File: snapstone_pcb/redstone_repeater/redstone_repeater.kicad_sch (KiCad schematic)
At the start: 0 parts

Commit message: Actual stuff is in the repeater file now
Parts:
- added C1, C2: 100 µF, symbol Device:C
- added C3: 150 µF, symbol Device:C
- added C4: 200 µF, symbol Device:C
- added R1: 500 ohms, symbol Device:R_US
- added R2, R3, R4: 1000 ohms, symbol Device:R_US
- added SW1, SW2, SW3, SW4: SW_Push, symbol Switch:SW_Push
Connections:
- new net: R2.1, SW2.2
- new net: C2.1, R2.2
- new net: R3.1, SW3.2
- new net: C3.1, R3.2
- new net: R1.1, SW1.2
- new net: C1.1, R1.2
- new net: SW1.1, SW2.1, SW3.1, SW4.1
- new net: C4.1, R4.2
- new net: R4.1, SW4.2
- new net GND: C1.2, C2.2, C3.2, C4.2

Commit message: Worked abit on the resistor
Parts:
- added C5: ~, symbol snapstone:3_Pin_Block_Connector
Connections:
- net GND: now also C5.2 (GND)
- net DAT: now reaches C2.1, R2.2
- net DAT: now also C1.1, C3.1, C4.1, R1.2, R3.2, R4.2
- net at SW1.1, SW2.1, SW3.1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: now also C5.3 (DAT)
- new net VCC: C5.1 (VCC)

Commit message: oops!
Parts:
- added C6, C7: ~, symbol snapstone:3_Pin_Block_Connector
- added R5: 150 ohms, symbol Device:R_US
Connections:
- net DAT: now also C6.3 (DAT)
- net GND: now also C6.2 (GND), C7.2 (GND)
- net VCC: now also C7.1 (VCC)
- new net: C7.3 (DAT), R5.1
- new net: C6.1 (VCC), R5.2

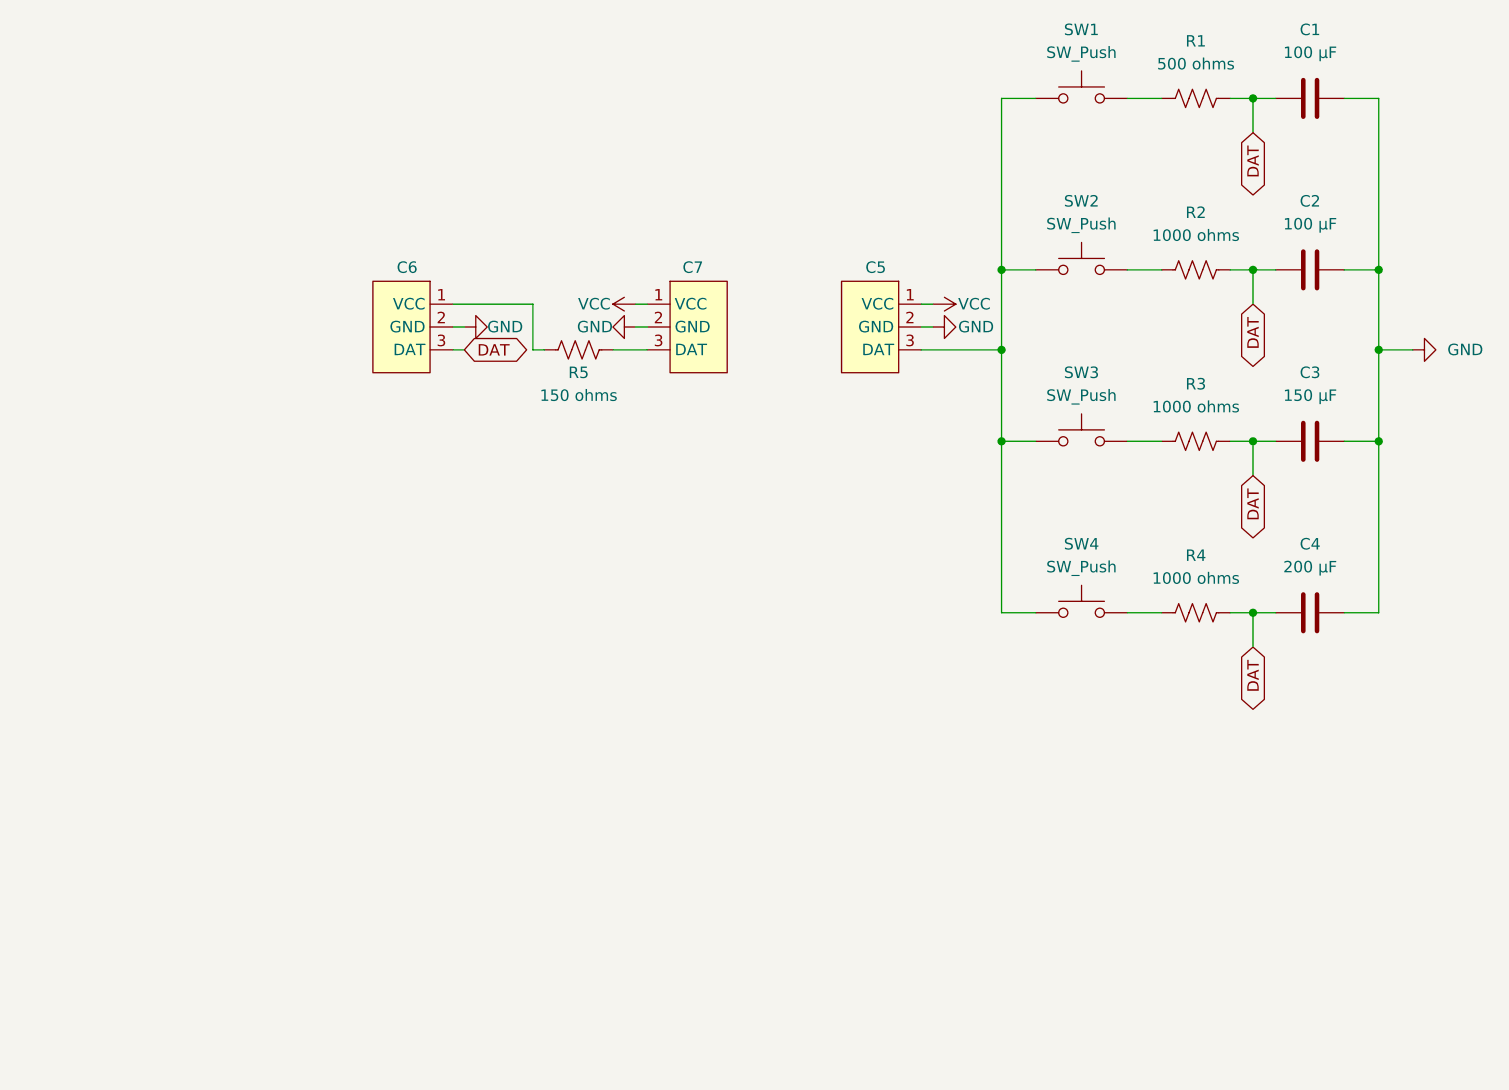
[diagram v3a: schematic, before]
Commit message: Worked on Comparator, gave it DigiPot, gave Repeater schematic a note
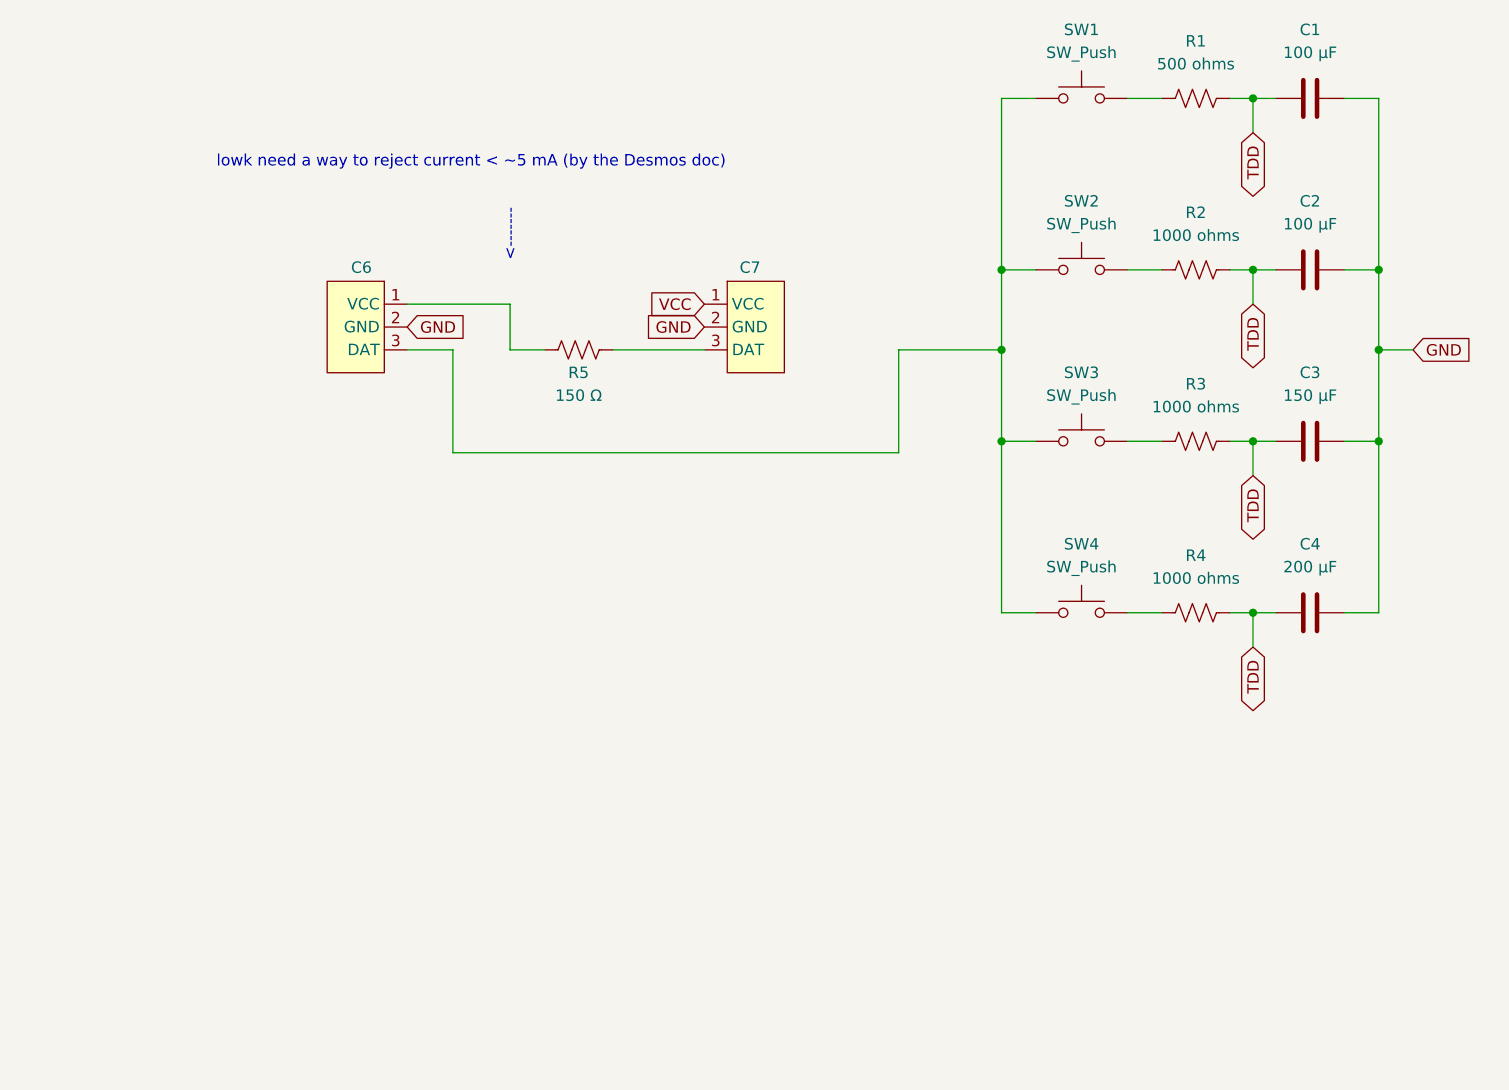
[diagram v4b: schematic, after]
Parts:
- removed C5: ~, symbol snapstone:3_Pin_Block_Connector
- R5: value 150 ohms -> 150 Ω
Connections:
- net at SW1.1, SW2.1, SW3.1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: now also C6.3 (DAT)
- net DAT renamed TDD
- net TDD: no longer C6.3 (DAT)
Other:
- note added: "<-------"
- note added: "lowk need a way to reject current < ~5 mA (by the Desmos doc)"
- moved on the sheet: C6, C7

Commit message: Polished up and maybe done repeater schematic????
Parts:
- added J1: ACS712 Current Sensor, symbol Connector:Conn_01x03_Socket
- added U1: MOUDLE-SEEEDUINO-XIAO, symbol XIAO_RP2040:MOUDLE-SEEEDUINO-XIAO
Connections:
- net GND: now also J1.3 (Pin_3), U1.13 (GND)
- net TDD: now also U1.2 (PA4_A1_D1)
- net VCC: now also C6.1 (VCC), R5.2, J1.1 (Pin_1), U1.12 (3V3)
- net DAT: now reaches C6.3 (DAT), SW1.1, SW2.1, SW3.1, SW4.1
- new net AOUT: J1.2 (Pin_2), U1.1 (PA02_A0_D0)
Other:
- note added: "CURRENT RESET"
- note added: "CURRENT SENSOR"
- note added: "DELAY SWITCH THING"
- note removed: "<-------"
- note removed: "lowk need a way to reject current < ~5 mA (by the Desmos doc)"
- moved on the sheet: C1, C2, C3, C4, C6, C7, R1, R2, R3, R4, R5, SW1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

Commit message: fixed DRC
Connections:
- no-connect marks 0 -> 10
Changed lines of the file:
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@@
+	)
+	(junction
+		(at 140.97 110.49)
+		(diameter 0)
+		(color 0 0 0 0)
 	)
 	(junction
@@
 	)
 	(junction
+		(at 140.97 113.03)
+		(diameter 0)
+		(color 0 0 0 0)
+	)
+	(junction
 		(at 171.45 93.98)
 		(diameter 0)
@@
 		(color 0 0 0 0)
 	)
+	(no_connect
+		(at 138.43 118.11)
+	)
+	(no_connect
+		(at 138.43 107.95)
+	)
+	(no_connect
+		(at 138.43 120.65)
+	)
+	(no_connect
+		(at 138.43 115.57)
+	)
+	(no_connect
+		(at 97.79 118.11)
+	)
+	(no_connect
+		(at 97.79 113.03)
+	)
+	(no_connect
+		(at 138.43 123.19)
+	)
+	(no_connect
+		(at 97.79 120.65)
+	)
+	(no_connect
+		(at 97.79 123.19)
+	)
+	(no_connect
+		(at 97.79 115.57)
+	)
 	(wire
 		(pts
@@
 	(wire
 		(pts
+			(xy 140.97 113.03) (xy 138.43 113.03)
+		)
+		(stroke
+			(width 0)
+			(type default)
+		)
+	)
+	(wire
+		(pts
 			(xy 199.39 104.14) (xy 201.93 104.14)
 		)
@@
 		(pts
 			(xy 171.45 93.98) (xy 171.45 104.14)
+		)
+		(stroke
+			(width 0)
+			(type default)
+		)
+	)
+	(wire
+		(pts
+			(xy 140.97 110.49) (xy 138.43 110.49)
 		)
 		(stroke
@@
 	(symbol
 		(lib_id "power:GND")
-		(at 138.43 110.49 90)
+		(at 140.97 110.49 90)
 		(unit 1)
 		(exclude_from_sim no)
@@
 		(fields_autoplaced yes)
 		(property "Reference" "#PWR03"
-			(at 144.78 110.49 0)
+			(at 147.32 110.49 0)
 			(effects
 				(font
@@
 		)
 		(property "Value" "GND"
-			(at 142.24 110.4899 90)
+			(at 144.78 110.4899 90)
 			(effects
 				(font
@@
 		)
 		(property "Footprint" ""
-			(at 138.43 110.49 0)
+			(at 140.97 110.49 0)
 			(effects
 				(font
@@
 		)
 		(property "Datasheet" ""
-			(at 138.43 110.49 0)
+			(at 140.97 110.49 0)
 			(effects
 				(font
@@
 		)
 		(property "Description" "Power symbol creates a global label with name \"GND\" , ground"
-			(at 138.43 110.49 0)
+			(at 140.97 110.49 0)
 			(effects
 				(font
@@
 	)
 	(symbol
-		(lib_id "power:VCC")
-		(at 138.43 113.03 270)
+		(lib_id "power:PWR_FLAG")
+		(at 140.97 113.03 180)
 		(unit 1)
 		(exclude_from_sim no)
@@
 		(on_board yes)
 		(dnp no)
+		(property "Reference" "#FLG02"
+			(at 140.97 114.935 0)
+			(effects
+				(font
+					(size 1.27 1.27)
+				)
+				(hide yes)
+			)
+		)
+		(property "Value" "PWR_FLAG"
+			(at 145.034 116.84 0)
+			(effects
+				(font
+					(size 1.27 1.27)
+				)
+			)
+		)
+		(property "Footprint" ""
+			(at 140.97 113.03 0)
+			(effects
+				(font
+					(size 1.27 1.27)
+				)
+				(hide yes)
+			)
+		)
+		(property "Datasheet" "~"
+			(at 140.97 113.03 0)
+			(effects
+				(font
+					(size 1.27 1.27)
+				)
+				(hide yes)
+			)
+		)
+		(property "Description" "Special symbol for telling ERC where power comes from"
+			(at 140.97 113.03 0)
+			(effects
+				(font
+					(size 1.27 1.27)
+				)
+				(hide yes)
+			)
+		)
+		(pin "1"
+		)
+		(instances
+			(project "redstone_repeater"
+				(path "/c6e4f295-c396-42f7-a6d5-97e88b8cc9c0"
+					(reference "#FLG02")
+					(unit 1)
+				)
+			)
+		)
+	)
+	(symbol
+		(lib_id "power:VCC")
+		(at 140.97 113.03 270)
+		(unit 1)
+		(exclude_from_sim no)
+		(in_bom yes)
+		(on_board yes)
+		(dnp no)
 		(fields_autoplaced yes)
 		(property "Reference" "#PWR04"
-			(at 134.62 113.03 0)
+			(at 137.16 113.03 0)
 			(effects
 				(font
@@
 		)
 		(property "Value" "VCC"
-			(at 142.24 113.0299 90)
+			(at 144.78 113.0299 90)
 			(effects
 				(font
@@
 		)
 		(property "Footprint" ""
-			(at 138.43 113.03 0)
+			(at 140.97 113.03 0)
 			(effects
 				(font
@@
 		)
 		(property "Datasheet" ""
-			(at 138.43 113.03 0)
+			(at 140.97 113.03 0)
 			(effects
 				(font
@@
 		)
 		(property "Description" "Power symbol creates a global label with name \"VCC\""
-			(at 138.43 113.03 0)
+			(at 140.97 113.03 0)
 			(effects
 				(font
@@
 					(unit 1)
 				)
+			)
+		)
+	)
+	(symbol
+		(lib_id "power:PWR_FLAG")
+		(at 140.97 110.49 0)
+		(unit 1)
+		(exclude_from_sim no)
+		(in_bom yes)
+		(on_board yes)
+		(dnp no)
+		(property "Reference" "#FLG01"
+			(at 140.97 108.585 0)
+			(effects
+				(font
+					(size 1.27 1.27)
+				)
+				(hide yes)
+			)
+		)
+		(property "Value" "PWR_FLAG"
+			(at 145.034 106.934 0)
+			(effects
+				(font
+					(size 1.27 1.27)
+				)
+			)
+		)
+		(property "Footprint" ""
+			(at 140.97 110.49 0)
+			(effects
+				(font
+					(size 1.27 1.27)
+				)
+				(hide yes)
+			)
+		)
+		(property "Datasheet" "~"
+			(at 140.97 110.49 0)
+			(effects
+				(font
+					(size 1.27 1.27)
+				)
+				(hide yes)
+			)
+		)
+		(property "Description" "Special symbol for telling ERC where power comes from"
+			(at 140.97 110.49 0)
+			(effects
+				(font
+					(size 1.27 1.27)
+				)
+				(hide yes)
+			)
+		)
+		(pin "1"
+		)
+		(instances
+			(project ""
+				(path "/c6e4f295-c396-42f7-a6d5-97e88b8cc9c0"
+					(reference "#FLG01")
+					(unit 1)
+				)

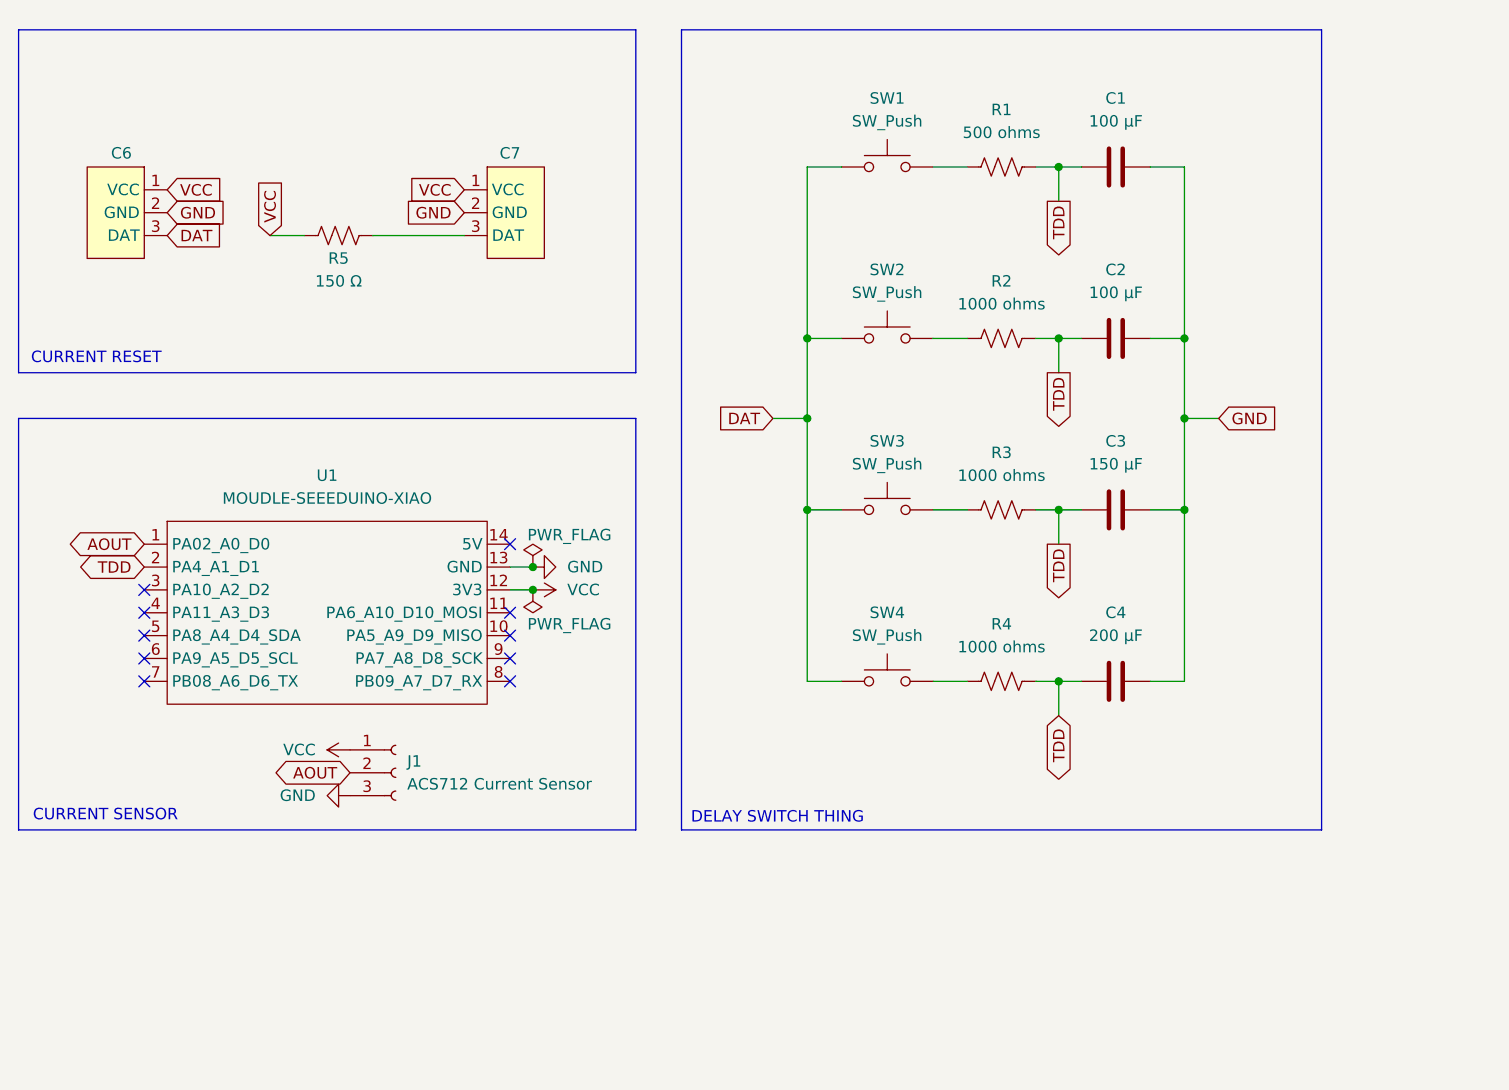
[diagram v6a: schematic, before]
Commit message: changed current sensor to TI chip in Repeater
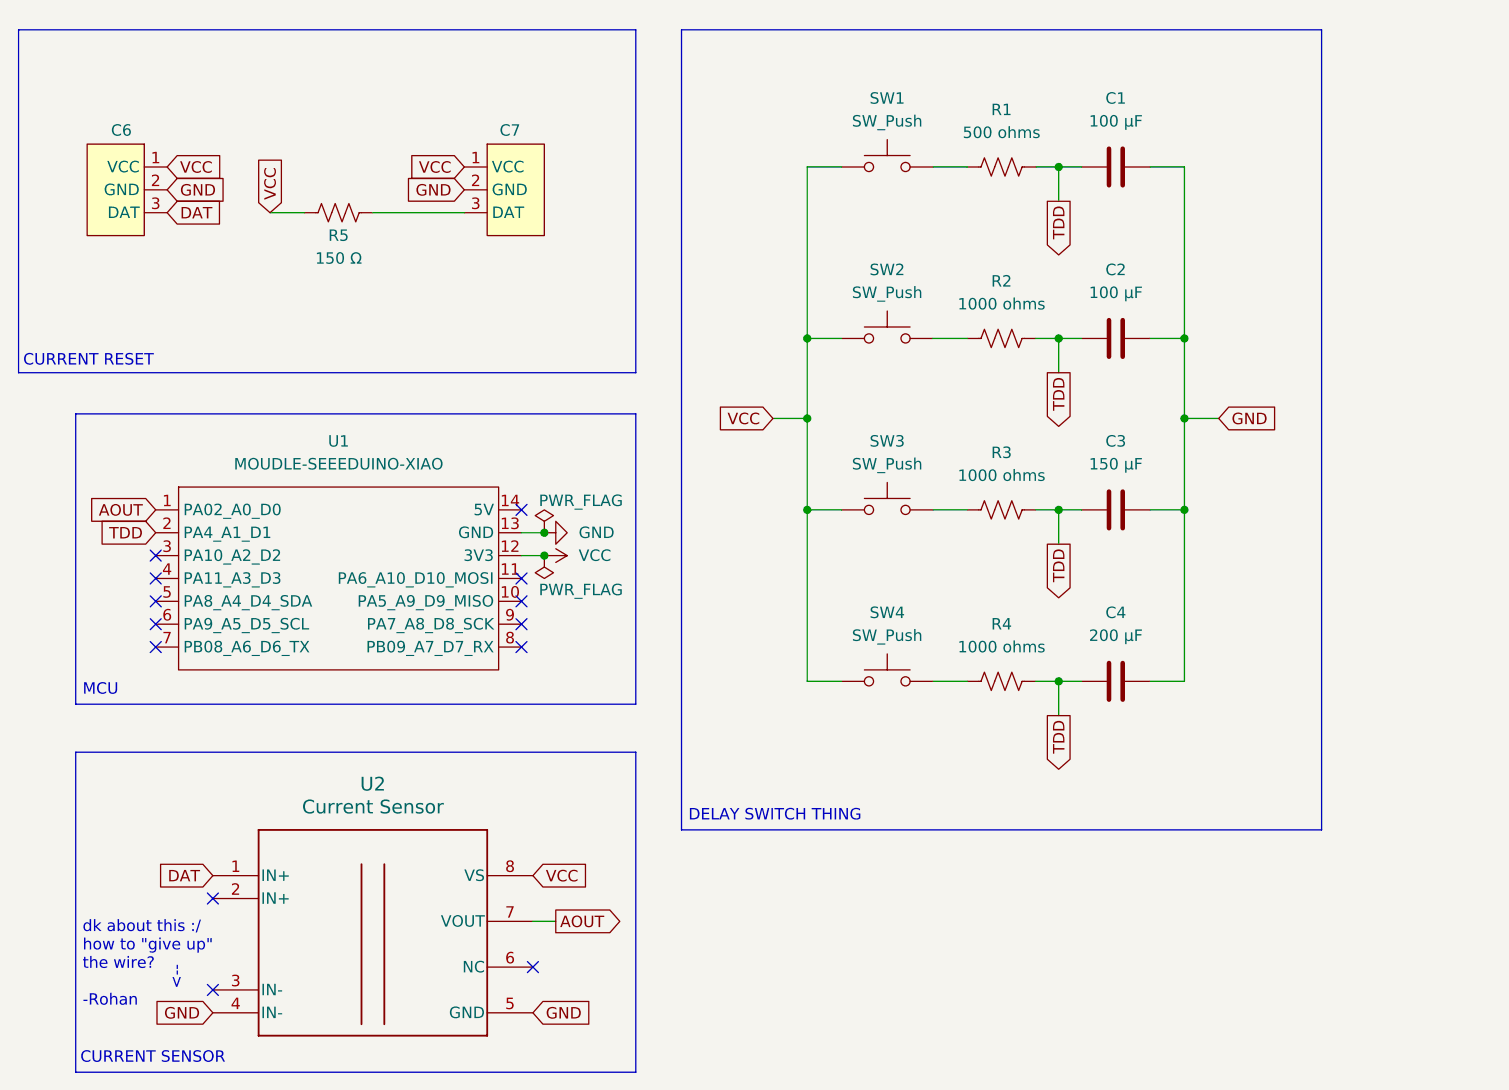
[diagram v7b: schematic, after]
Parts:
- removed J1: ACS712 Current Sensor, symbol Connector:Conn_01x03_Socket
- added U2: Current Sensor, TMCS1108A2UQDR_Current_Sensor:D0008A-IPC_A, symbol TMCS1108A2UQDR_Current_Sensor:TMCS1108A2UQDR
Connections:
- net AOUT: now also U2.7 (VOUT)
- net DAT: now also U2.1 (IN+); no longer SW1.1, SW2.1, SW3.1, SW4.1
- net GND: now also U2.4 (IN-), U2.5 (GND)
- net VCC: now also SW1.1, SW2.1, SW3.1, SW4.1, U2.8 (VS)
- no-connect marks 10 -> 13
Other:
- note added: "<--"
- note added: "MCU"
- note added: "dk about this :/ how to "give up" the wire? -Rohan"
- moved on the sheet: C6, C7, R5, U1

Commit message: Final touchups with ohms
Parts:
- R1: value 500 ohms -> 500 Ω
- R2, R3, R4: value 1000 ohms -> 1000 Ω
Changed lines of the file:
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@@
 			)
 		)
-		(property "Value" "1000 ohms"
+		(property "Value" "1000 Ω"
 			(at 193.04 81.28 90)
 			(effects
@@
 			)
 		)
-		(property "Value" "1000 ohms"
+		(property "Value" "1000 Ω"
 			(at 193.04 100.33 90)
 			(effects
@@
 			)
 		)
-		(property "Value" "500 ohms"
+		(property "Value" "500 Ω"
 			(at 193.04 62.23 90)
 			(effects
@@
 			)
 		)
-		(property "Value" "1000 ohms"
+		(property "Value" "1000 Ω"
 			(at 193.04 119.38 90)
 			(effects
